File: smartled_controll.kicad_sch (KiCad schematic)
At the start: 91 parts, among them J1 Conn_01x04, SW1 SW_Push, U1 OC5028B, U2 MAX485E, U3 PY32F003F1xUx, U4 OC5864, U5 need chooice, U6 OC5028B, U7 need chooice, U8 OC5028B, U9 OC5028B, Y1 Crystal_GND23

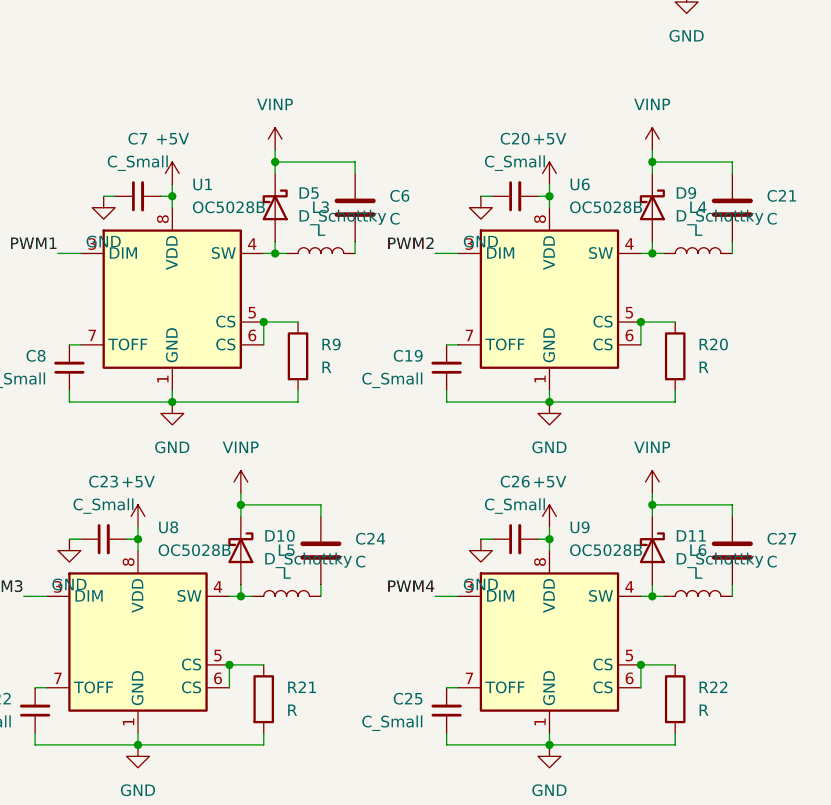
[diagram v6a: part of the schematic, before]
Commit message: 添加LED驱动输入滤波电容(1210封装)
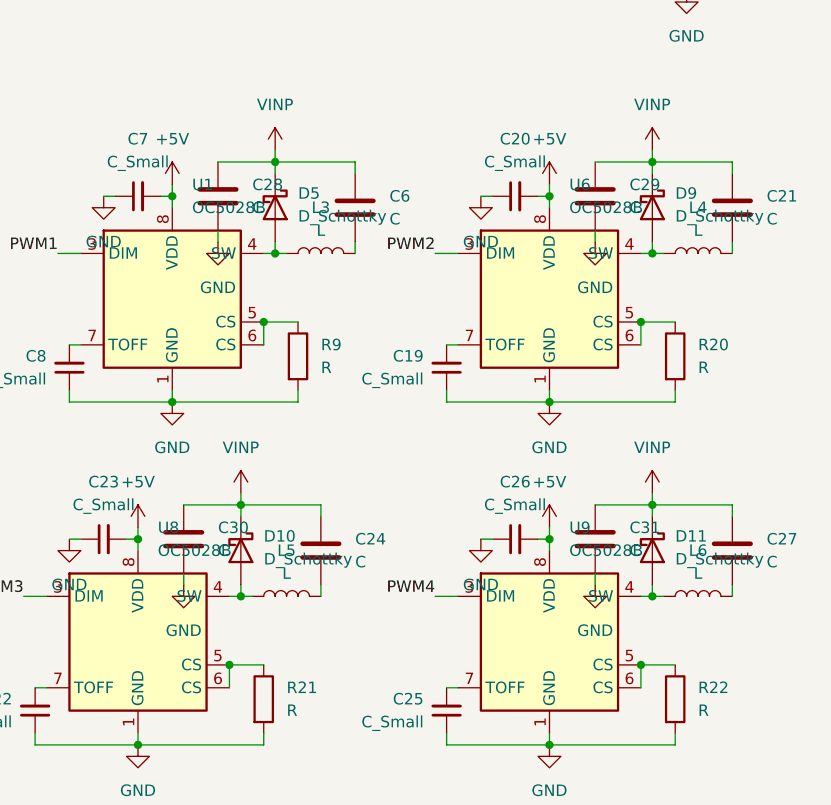
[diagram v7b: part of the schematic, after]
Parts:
- added C28, C29, C30, C31: C, Capacitor_SMD:C_1210_3225Metric, symbol Device:C
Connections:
- net GND: now also C28.1, C29.1, C30.1, C31.1
- net VINP: now also C28.2, C29.2, C30.2, C31.2

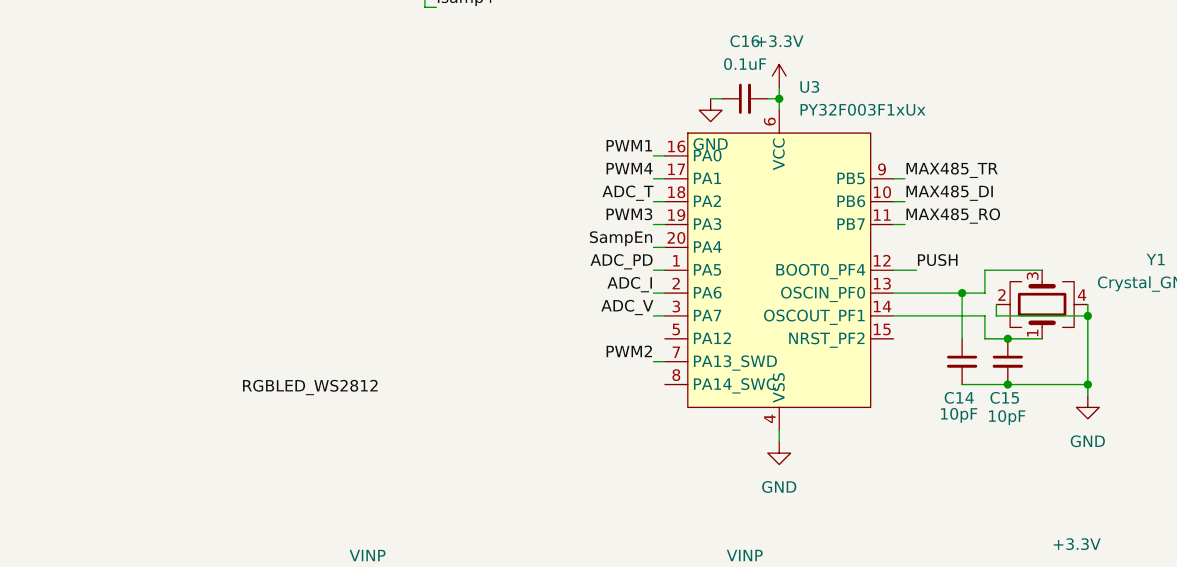
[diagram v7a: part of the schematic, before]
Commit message: 添加I2C接口
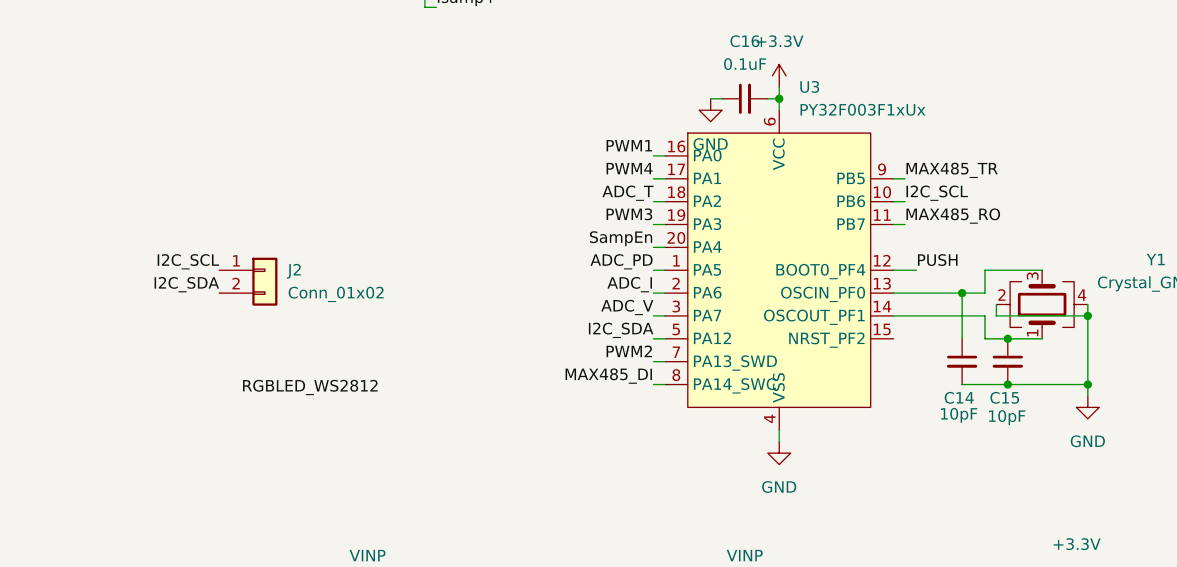
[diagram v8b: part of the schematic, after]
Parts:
- added J2: Conn_01x02, Resistor_SMD:R_0603_1608Metric, symbol Connector_Generic:Conn_01x02
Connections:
- net MAX485_DI: now also U3.8 (PA14_SWC); no longer U3.10 (PB6)
- net I2C_SDA: now reaches U3.5 (PA12)
- net I2C_SDA: now also J2.2 (Pin_2)
- new net I2C_SCL: J2.1 (Pin_1), U3.10 (PB6)
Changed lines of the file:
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@@
 	(wire
 		(pts
+			(xy 81.28 101.6) (xy 82.55 101.6)
+		)
+		(stroke
+			(width 0)
+			(type default)
+		)
+	)
+	(wire
+		(pts
 			(xy 172.72 71.12) (xy 172.72 72.39)
 		)
@@
 	(wire
 		(pts
+			(xy 81.28 96.52) (xy 82.55 96.52)
+		)
+		(stroke
+			(width 0)
+			(type default)
+		)
+	)
+	(wire
+		(pts
 			(xy 161.29 87.63) (xy 162.56 87.63)
 		)
@@
 		)
 	)
-	(label "MAX485_DI"
-		(at 109.22 81.28 0)
-		(effects
-			(font
-				(size 1.27 1.27)
-			)
-			(justify left bottom)
-		)
-	)
 	(label "VIN+"
 		(at 22.86 34.29 180)
@@
 		)
 	)
+	(label "I2C_SDA"
+		(at 33.02 91.44 180)
+		(effects
+			(font
+				(size 1.27 1.27)
+			)
+			(justify right bottom)
+		)
+	)
 	(label "PUSH"
 		(at 130.81 137.16 0)
@@
 		)
 	)
+	(label "I2C_SCL"
+		(at 33.02 88.9 180)
+		(effects
+			(font
+				(size 1.27 1.27)
+			)
+			(justify right bottom)
+		)
+	)
 	(label "ADC_PD"
 		(at 81.28 88.9 180)
@@
 		)
 	)
+	(label "MAX485_DI"
+		(at 81.28 101.6 180)
+		(effects
+			(font
+				(size 1.27 1.27)
+			)
+			(justify right bottom)
+		)
+	)
 	(label "RGBLED_WS2812"
 		(at 50.8 102.87 180)
@@
 		)
 	)
+	(label "I2C_SCL"
+		(at 109.22 81.28 0)
+		(effects
+			(font
+				(size 1.27 1.27)
+			)
+			(justify left bottom)
+		)
+	)
 	(label "ADC_T"
 		(at 171.45 137.16 0)
@@
 		)
 	)
+	(label "I2C_SDA"
+		(at 81.28 96.52 180)
+		(effects
+			(font
+				(size 1.27 1.27)
+			)
+			(justify right bottom)
+		)
+	)
 	(label "PWM1"
 		(at 25.4 137.16 180)
@@
 					(unit 1)
 				)
+			)
+		)
+	)
+	(symbol
+		(lib_id "Connector_Generic:Conn_01x02")
+		(at 38.1 88.9 0)
+		(unit 1)
+		(exclude_from_sim no)
+		(in_bom yes)
+		(on_board yes)
+		(dnp no)
+		(fields_autoplaced yes)
+		(property "Reference" "J2"
+			(at 40.64 88.8999 0)
+			(effects
+				(font
+					(size 1.27 1.27)
+				)
+				(justify left)
+			)
+		)
+		(property "Value" "Conn_01x02"
+			(at 40.64 91.4399 0)
+			(effects
+				(font
+					(size 1.27 1.27)
+				)
+				(justify left)
+			)
+		)
+		(property "Footprint" "Resistor_SMD:R_0603_1608Metric"
+			(at 38.1 88.9 0)
+			(effects
+				(font
+					(size 1.27 1.27)
+				)
+				(hide yes)
+			)
+		)
+		(property "Datasheet" "~"
+			(at 38.1 88.9 0)
+			(effects
+				(font
+					(size 1.27 1.27)
+				)
+				(hide yes)
+			)
+		)
+		(property "Description" "Generic connector, single row, 01x02, script generated (kicad-library-utils/schlib/autogen/connector/)"
+			(at 38.1 88.9 0)
+			(effects
+				(font
+					(size 1.27 1.27)
+				)
+				(hide yes)
+			)
+		)
+		(pin "1"
+		)
+		(pin "2"
+		)
+		(instances
+			(project ""
+				(path "/b299fa7e-4ddc-4ca9-9929-510e6cf892c6"
+					(reference "J2")
+					(unit 1)
+				)
